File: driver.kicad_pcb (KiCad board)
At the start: 2 copper layers, 96 x 45 mm, 73 parts, among them P1 CONN_01X02, P101 CONN_02X02, P151 CONN_02X02, P2 TL431, P201 CONN_02X02, P3 LM335, P51 CONN_02X02, Q1 Q_NMOS_GSD, Q101 TIP122, Q102 TIP122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

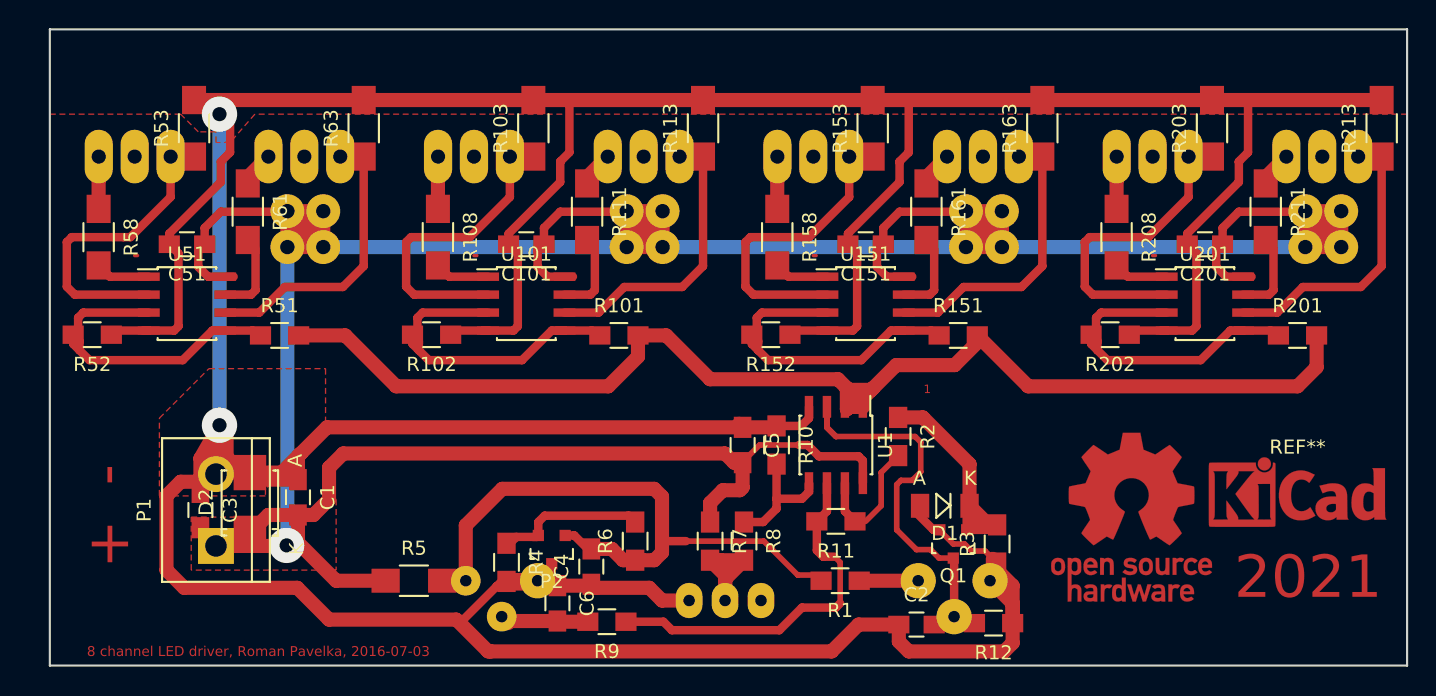
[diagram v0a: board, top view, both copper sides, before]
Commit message: Add labels for potentiometers
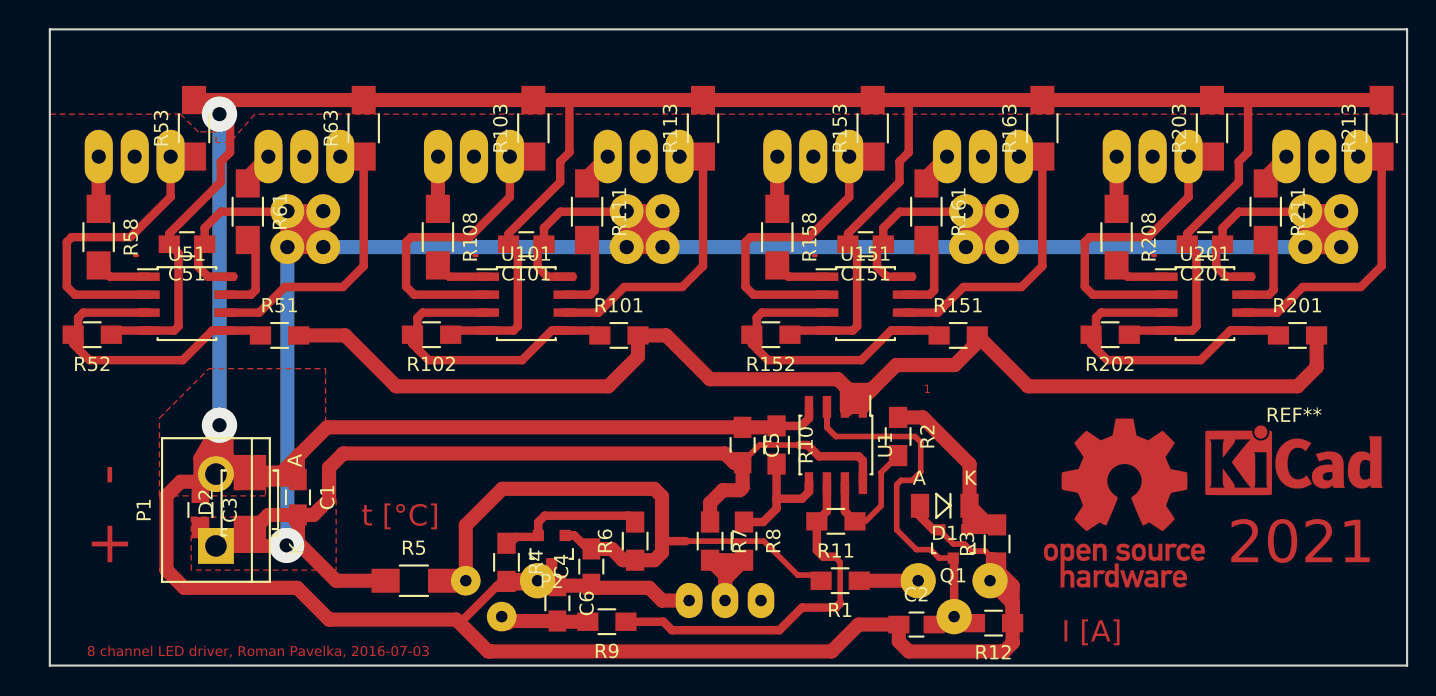
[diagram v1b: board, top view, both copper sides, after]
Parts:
- moved REF** 2.26 mm to (188.5, 113.5)
- moved REF** 1.12 mm to (176.5, 116.0)
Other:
- board text added: "I [A]"
- board text added: "t [°C]"
